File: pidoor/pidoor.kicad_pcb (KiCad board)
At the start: 2 copper layers, 50 x 28 mm, 36 parts, among them K1 RELAY_G6L, P1 CONN_02X13, P2 PWR, P3 IN0, P4 IN1, P5 IN2, P6 READER, P7 MAG, Q1 PMV16XN, Q2 PMV16XN, Q3 PMV16XN, U1 MIC5317-3.3YM5, U2 ST3232BDR

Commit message: previews
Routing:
- net +3V3: track 19.7 -> 44.1 mm, vias 0 -> 2
- net /12_EMG: track 35.5 -> 44.8 mm
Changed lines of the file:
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@@
   (general
     (links 80)
-    (no_connects 1)
-    (area 127.924999 114.924999 178.075001 143.075001)
+    (no_connects 0)
+    (area 124.049999 106.325 242.964763 187.88)
     (thickness 1.6)
     (drawings 65)
-    (tracks 192)
+    (tracks 206)
     (zones 0)
     (modules 36)
@@
     (visible_elements 7FFFFFFF)
     (pcbplotparams
-      (layerselection 0x010f0_80000001)
+      (layerselection 0x010ff_80000001)
       (usegerberextensions true)
       (excludeedgelayer true)
@@
       (drillshape 0)
       (scaleselection 1)
-      (outputdirectory ""))
+      (outputdirectory out/))
   )
   (net 0 "")
@@
   (segment (start 142.75 127.66) (end 142.85 127.76) (width 0.4) (layer B.Cu) (net 1) (status 30))
   (segment (start 142.85 127.76) (end 145.8 127.76) (width 0.4) (layer B.Cu) (net 1) (status 30))
+  (segment (start 139.8 133.76) (end 139.8 135.76) (width 0.4) (layer B.Cu) (net 3))
+  (segment (start 160.245 133.56) (end 160.245 134.565) (width 0.4) (layer B.Cu) (net 3))
+  (segment (start 160.245 134.565) (end 157.55 137.26) (width 0.4) (layer B.Cu) (net 3))
+  (segment (start 157.55 137.26) (end 150.3 137.26) (width 0.4) (layer B.Cu) (net 3))
+  (segment (start 150.3 137.26) (end 149.8 137.76) (width 0.4) (layer B.Cu) (net 3))
+  (via (at 149.8 137.76) (size 1) (drill 0.6) (layers F.Cu B.Cu) (net 3))
+  (segment (start 149.8 137.76) (end 142.3 137.76) (width 0.4) (layer F.Cu) (net 3))
+  (segment (start 142.3 137.76) (end 140.55 136.01) (width 0.4) (layer F.Cu) (net 3))
+  (via (at 140.55 136.01) (size 1) (drill 0.6) (layers F.Cu B.Cu) (net 3))
+  (segment (start 140.55 136.01) (end 140.3 135.76) (width 0.4) (layer B.Cu) (net 3))
+  (segment (start 140.3 135.76) (end 139.8 135.76) (width 0.4) (layer B.Cu) (net 3))
+  (segment (start 139.8 135.76) (end 138.55 135.76) (width 0.4) (layer B.Cu) (net 3))
   (segment (start 162.3 133.51) (end 160.295 133.51) (width 0.4) (layer B.Cu) (net 3))
   (segment (start 160.295 133.51) (end 160.245 133.56) (width 0.4) (layer B.Cu) (net 3))
@@
   (segment (start 141.05 131.76) (end 140.85 131.56) (width 0.4) (layer B.Cu) (net 3) (status 30))
   (segment (start 140.85 131.56) (end 140.85 129.86) (width 0.4) (layer B.Cu) (net 3) (status 30))
-  (segment (start 138.55 135.76) (end 139.8 134.51) (width 0.4) (layer B.Cu) (net 3) (status 10))
-  (segment (start 139.8 134.51) (end 139.8 129.86) (width 0.4) (layer B.Cu) (net 3))
+  (segment (start 139.8 133.76) (end 139.8 129.86) (width 0.4) (layer B.Cu) (net 3))
   (segment (start 138.55 123.76) (end 139.8 125.01) (width 0.4) (layer B.Cu) (net 3) (status 10))
   (segment (start 138.55 129.76) (end 138.65 129.86) (width 0.4) (layer B.Cu) (net 3) (status 30))
@@
   (segment (start 168.3 125.51) (end 168.3 125.58) (width 0.4) (layer B.Cu) (net 26) (status 30))
   (segment (start 166.15 127.66) (end 166.08 127.73) (width 0.4) (layer B.Cu) (net 26) (status 30))
+  (segment (start 149.8 139.26) (end 151.45 139.26) (width 0.4) (layer F.Cu) (net 27))
+  (segment (start 151.45 139.26) (end 159.77 130.94) (width 0.4) (layer F.Cu) (net 27))
+  (segment (start 151.355 138.96) (end 150.1 138.96) (width 0.4) (layer B.Cu) (net 27))
+  (segment (start 153.8 136.76) (end 153.8 136.91) (width 0.4) (layer F.Cu) (net 27))
+  (segment (start 151.45 139.26) (end 151.45 139.11) (width 0.4) (layer F.Cu) (net 27))
+  (segment (start 151.45 139.11) (end 153.8 136.76) (width 0.4) (layer F.Cu) (net 27))
+  (via (at 149.8 139.26) (size 1) (drill 0.6) (layers F.Cu B.Cu) (net 27))
+  (segment (start 150.1 138.96) (end 149.8 139.26) (width 0.4) (layer B.Cu) (net 27))
   (segment (start 163.05 122.76) (end 163.05 123.81) (width 0.4) (layer F.Cu) (net 27))
-  (segment (start 152.95 137.76) (end 149.8 137.76) (width 0.4) (layer F.Cu) (net 27))
-  (segment (start 159.77 130.94) (end 152.95 137.76) (width 0.4) (layer F.Cu) (net 27))
+  (segment (start 163.05 123.81) (end 159.77 127.09) (width 0.4) (layer F.Cu) (net 27))
   (segment (start 159.77 127.09) (end 159.77 130.94) (width 0.4) (layer F.Cu) (net 27))
-  (segment (start 163.05 123.81) (end 159.77 127.09) (width 0.4) (layer F.Cu) (net 27))
-  (segment (start 151.355 138.96) (end 151 138.96) (width 0.4) (layer B.Cu) (net 27))
-  (segment (start 151 138.96) (end 149.8 137.76) (width 0.4) (layer B.Cu) (net 27))
-  (via (at 149.8 137.76) (size 1) (drill 0.6) (layers F.Cu B.Cu) (net 27))
-  (segment (start 149.8 137.76) (end 152.8 137.76) (width 0.4) (layer F.Cu) (net 27))
+  (segment (start 159.77 130.94) (end 153.8 136.91) (width 0.4) (layer F.Cu) (net 27))
   (segment (start 163.05 122.76) (end 162.65 122.36) (width 0.4) (layer F.Cu) (net 27))
   (segment (start 162.65 122.36) (end 162.65 119.5) (width 0.4) (layer F.Cu) (net 27))

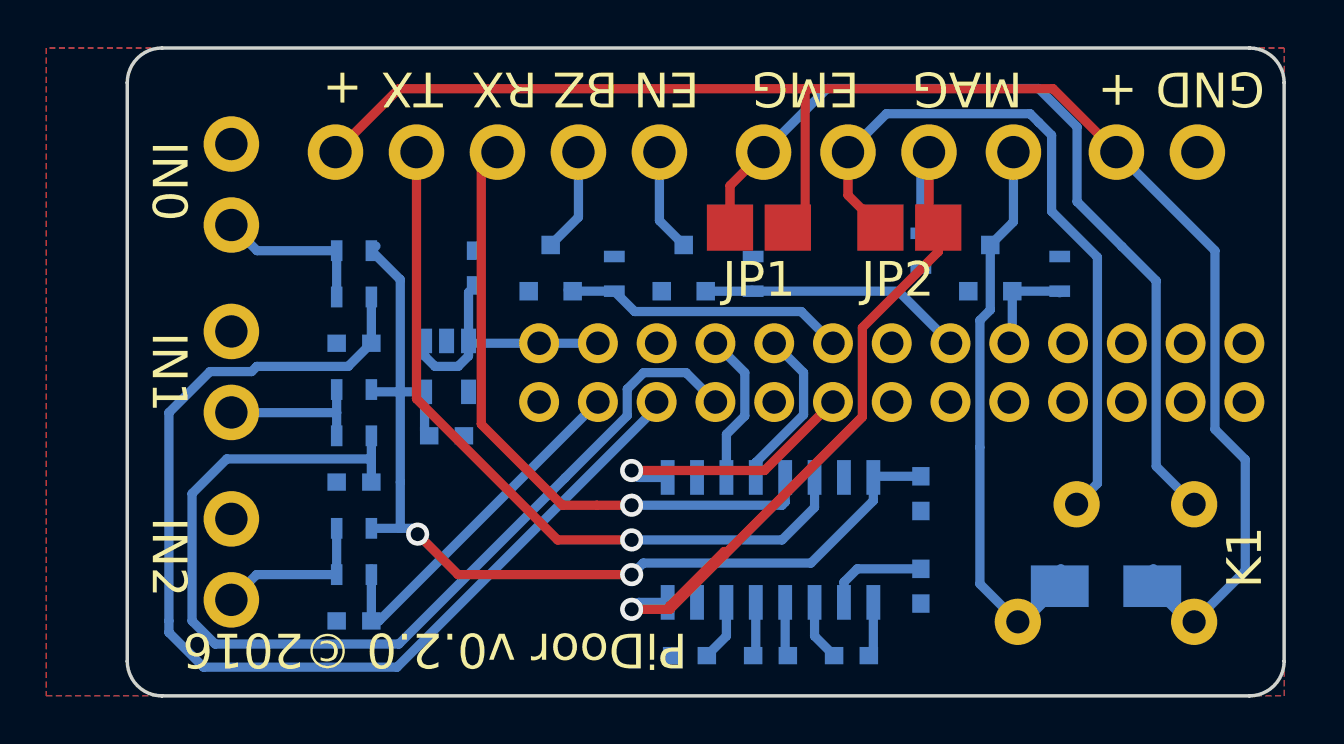
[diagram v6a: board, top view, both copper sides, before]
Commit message: gnd unused inputs
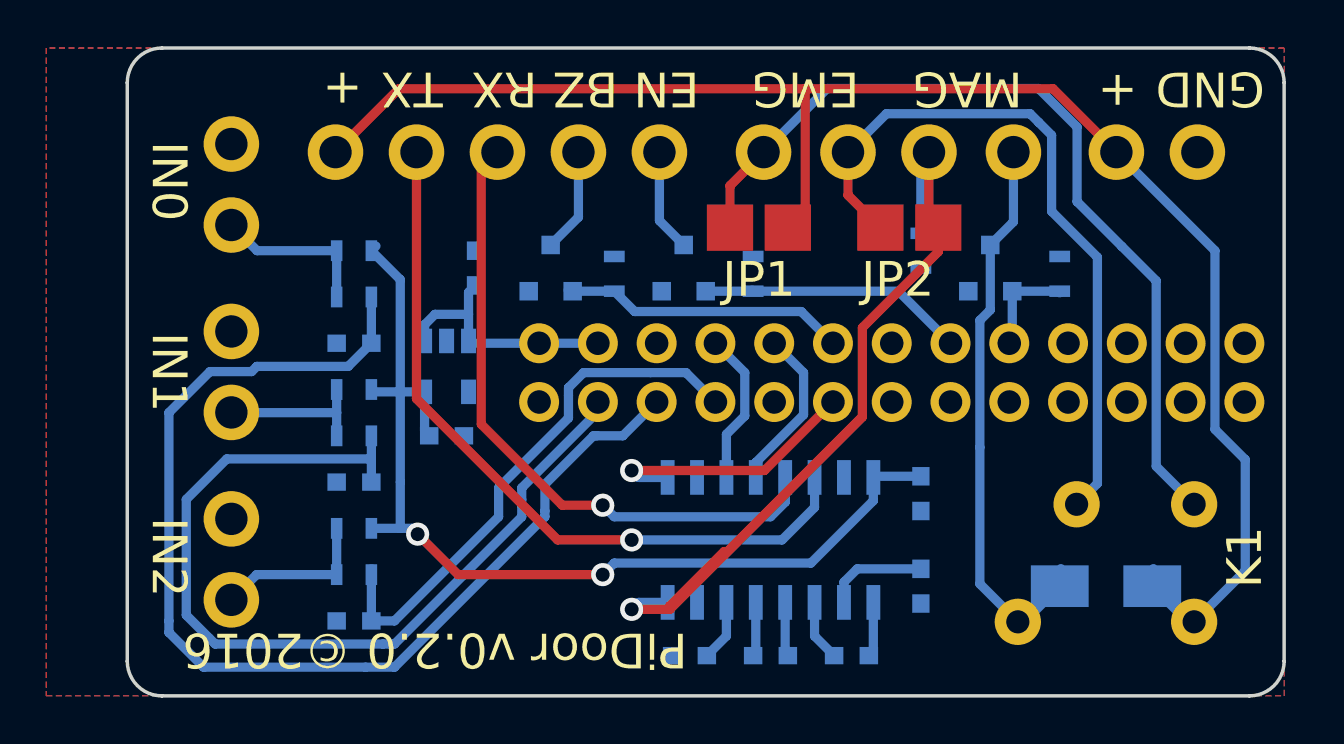
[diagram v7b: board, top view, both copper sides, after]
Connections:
- P1 pad 3: /IN2 -> /IN1
- P1 pad 7: /IN1 -> /IN2
- U2 pad 10: (no net) -> GND
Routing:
- net /IN2: track 16.0 -> 23.8 mm
- net /IN1: track 45.0 -> 39.8 mm
- net /EIA-RX: track 27.8 -> 29.2 mm
- net /IN0: track 48.2 -> 49.1 mm
- net +5V: track 11.7 -> 10.9 mm

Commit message: pre-production tweeks
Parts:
- D1: footprint Diodes_SMD:SMA_Standard -> Diodes_SMD:SOD-123
- K1: moved to B.Cu
- moved D1 2.50 mm to (170.3, 140.8)
- moved K1 1.00 mm to (170.3, 136.3)
- moved R10 1.00 mm to (162.3, 124.8)
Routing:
- net /12_EMG: track 44.8 -> 33.7 mm
- net +12V: track 69.4 -> 67.8 mm
- net Net-(D1-Pad2): track 24.9 -> 23.6 mm
- net Net-(JP2-Pad1): track 30.9 -> 29.9 mm
- net Net-(JP1-Pad1): track 37.6 -> 36.6 mm
